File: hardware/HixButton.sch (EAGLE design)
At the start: 16 parts, among them J1 FTDI, J3 XH2P

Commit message: hardware update
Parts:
- removed AWAKE: (no value), jumper:SJ
- removed J3: XH2P, 0_HixField:XH2P
- added C1: 100nF, rcl:C-EUC1206
- added JMP1: (no value), jumper:SJ
- added L1: GRN, led:LEDCHIPLED_1206
- added L2: RED, led:LEDCHIPLED_1206
- added LIFEPO4, WAKE: XH2P, 0_HixField:XH2P
- added R3, R4: 10K, rcl:R-EU_R1206
- added U$1: CN3058E, 0_HixField:CN3058E
- added U1: TPS3839L30, 0_HixField:TPS3839
- added X1: MINI-USB_SHIELD5P4-32005-400, con-cypressindustries:MINI-USB_SHIELD5P4-32005-400
- C2: value 47μF -> 1uF; device rcl:CPOL-EUSMCA -> rcl:C-EUC1206
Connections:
- removed net N$7: R10.1, S3.1, U$2.RST
- new net N$10: C2.1, R4.2, U$1.VIN, X1G$1.1
- new net N$11: L1.A, L2.A, R4.1
- new net N$12: L2.C, U$1.CHRG
- new net N$13: L1.C, U$1.DONE
- new net N$5: R10.1, S3.2, U$2.RST, WAKE.1
- new net N$6: R3.2, U$1.ISET
- new net N$9: S3.1, U1.RST, WAKE.2
- net 3.3V: now also C1.1, LIFEPO4.2, U$1.BAT, U$1.FB, U1.VDD; no longer C2.+, J3.2
- net GND: now also C1.2, C2.2, JMP1.1, LIFEPO4.1, R3.1, U$1.GND, U$1.TEMP, U1.GND, X1G$1.4; no longer AWAKE.1, C2.-, J3.1, S3.2
- net N$4: now also JMP1.2; no longer AWAKE.2
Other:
- moved on the sheet: C3, C5, C6, J1, R1, R10, R11, R12, R2, S3, S4, U$2

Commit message: updated hardware board and schematic
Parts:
- removed U$3: LED_RGB, 0_HixField:LED_RGB
- added U4: LED_RGBWS2812_5050, 0_HixField:LED_RGBWS2812_5050
- R3: value 10K -> 1.2K
- R4: value 10K -> 330
- renumbered U$1 to U2, U$2 to U3
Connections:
- net N$10 renamed VIN
- net 3.3V: now also U4.VCC; no longer U$3.VCC
- net GND: now also U4.GND; no longer U$3.GND
- net RGB: now also U4.DIN; no longer U$3.DIN

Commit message: updated hardware
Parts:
- removed S4: PROG, 0_HixField:PUSHBTNSMALL
- added C10: 1uF, rcl:C-EUC1206
- added C4: 100nF, rcl:C-EUC1206
- added C7, C8, C9: 100μF, rcl:CPOL-EUSMCA
- added PROG: (no value), jumper:SJ
- C2: value 1uF -> 100nF
- C5: value 100nF -> 100μF; device rcl:C-EUC1206 -> rcl:CPOL-EUSMCA; SPICEPREFIX C -> (none)
- C6: value 680μF/6.3V -> 100μF; device 0_HixField:ELCOELKO_RADIAL_STRAIGHT_4P_8D_9H -> rcl:CPOL-EUSMCA
- U1: value TPS3839L30 -> ESP8266(ESP12E)V2; device 0_HixField:TPS3839 -> 0_HixField:ESP8266(ESP12E)V2
- U2: value CN3058E -> TPS3839L30; device 0_HixField:CN3058E -> 0_HixField:TPS3839
- U3: value ESP8266(ESP12E)V2 -> CN3058E; device 0_HixField:ESP8266(ESP12E)V2 -> 0_HixField:CN3058E
- renumbered JMP1 to STAYAWAKE
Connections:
- net 3.3V: now also C2.1, C4.1, C5.+, C7.+, C8.+, C9.+, U1.VCC, U2.VDD, U3.BAT, U3.FB; no longer C5.1, U1.VDD, U2.BAT, U2.FB, U3.VCC
- net GND: now also C10.2, C4.2, C5.-, C7.-, C8.-, C9.-, PROG.1, U3.TEMP; no longer C5.2, S4.2, U2.TEMP
- net N$1: now also U1.CS_TXD2_GPIO15; no longer U3.CS_TXD2_GPIO15
- net N$12: now also U3.CHRG; no longer U2.CHRG
- net N$13: now also U3.DONE; no longer U2.DONE
- net N$2: now also U1.TXD1_GPIO2; no longer U3.TXD1_GPIO2
- net N$3: now also PROG.2, U1.FLASH_GPIO0; no longer S4.1, U3.FLASH_GPIO0
- net N$4: now also U1.SDA_GPIO4; no longer U3.SDA_GPIO4
- net N$5: now also U1.RST; no longer U3.RST
- net N$6: now also U3.ISET; no longer U2.ISET
- net N$8: now also U1.ENABLE; no longer U3.ENABLE
- net N$9: now also U2.RST; no longer U1.RST
- net RGB: now also U1.SCL_GPIO5; no longer U3.SCL_GPIO5
- net RXD: now also U1.TXD0_GPIO1; no longer U3.TXD0_GPIO1
- net TXD: now also U1.RXD0_GPIO3; no longer U3.RXD0_GPIO3
- net VIN: now also C10.1, U3.VIN; no longer C2.1, U2.VIN
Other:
- moved on the sheet: C1, C2, C3, C6, L1, L2, LIFEPO4, R3, R4, X1

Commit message: updated sch and board layout
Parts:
- removed X1: MINI-USB_SHIELD5P4-32005-400, con-cypressindustries:MINI-USB_SHIELD5P4-32005-400
- R3: value 1.2K -> 5.6K
- U4: value LED_RGBWS2812_5050 -> WS2812
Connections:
- removed net VIN: C10.1, R4.2, U3.VIN, X1G$1.1
- new net 5.0V: C10.1, J1.5V, R4.2, U3.VIN
- net 3.3V: no longer J1.5V
- net GND: no longer X1G$1.4
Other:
- moved on the sheet: C10

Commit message: orderd pcbs
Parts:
- renumbered L1 to L1(GRN), L2 to L2(RED)
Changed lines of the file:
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@@
 </part>
 <part name="GND10" library="supply1" library_urn="urn:adsk.eagle:library:371" deviceset="GND" device=""/>
-<part name="L2" library="led" library_urn="urn:adsk.eagle:library:259" deviceset="LED" device="CHIPLED_1206" package3d_urn="urn:adsk.eagle:package:15823/2" value="RED"/>
-<part name="L1" library="led" library_urn="urn:adsk.eagle:library:259" deviceset="LED" device="CHIPLED_1206" package3d_urn="urn:adsk.eagle:package:15823/2" value="GRN"/>
+<part name="L2(RED)" library="led" library_urn="urn:adsk.eagle:library:259" deviceset="LED" device="CHIPLED_1206" package3d_urn="urn:adsk.eagle:package:15823/2" value="RED"/>
+<part name="L1(GRN)" library="led" library_urn="urn:adsk.eagle:library:259" deviceset="LED" device="CHIPLED_1206" package3d_urn="urn:adsk.eagle:package:15823/2" value="GRN"/>
 <part name="R4" library="rcl" library_urn="urn:adsk.eagle:library:334" deviceset="R-EU_" device="R1206" package3d_urn="urn:adsk.eagle:package:23540/2" value="330"/>
 <part name="GND8" library="supply1" library_urn="urn:adsk.eagle:library:371" deviceset="GND" device=""/>
@@
 <attribute name="VALUE" x="60.96" y="68.58" size="1.778" layer="96"/>
 </instance>
-<instance part="L2" gate="G$1" x="86.36" y="101.6" smashed="yes">
+<instance part="L2(RED)" gate="G$1" x="86.36" y="101.6" smashed="yes">
 <attribute name="NAME" x="89.662" y="104.14" size="1.778" layer="95" rot="R180"/>
 <attribute name="VALUE" x="91.948" y="97.663" size="1.778" layer="96" rot="R180"/>
 </instance>
-<instance part="L1" gate="G$1" x="76.2" y="101.6" smashed="yes">
+<instance part="L1(GRN)" gate="G$1" x="76.2" y="101.6" smashed="yes">
 <attribute name="NAME" x="75.184" y="104.14" size="1.778" layer="95" rot="R180"/>
 <attribute name="VALUE" x="75.692" y="97.409" size="1.778" layer="96" rot="R180"/>
@@
 <segment>
 <pinref part="R4" gate="G$1" pin="1"/>
-<pinref part="L2" gate="G$1" pin="A"/>
+<pinref part="L2(RED)" gate="G$1" pin="A"/>
 <wire x1="81.28" y1="104.14" x2="86.36" y2="104.14" width="0.1524" layer="91"/>
-<pinref part="L1" gate="G$1" pin="A"/>
+<pinref part="L1(GRN)" gate="G$1" pin="A"/>
 <wire x1="81.28" y1="104.14" x2="76.2" y2="104.14" width="0.1524" layer="91"/>
 <junction x="81.28" y="104.14"/>
@@
 <net name="N$12" class="2">
 <segment>
-<pinref part="L2" gate="G$1" pin="C"/>
+<pinref part="L2(RED)" gate="G$1" pin="C"/>
 <wire x1="86.36" y1="96.52" x2="86.36" y2="93.98" width="0.1524" layer="91"/>
 <wire x1="86.36" y1="93.98" x2="91.44" y2="93.98" width="0.1524" layer="91"/>
@@
 <net name="N$13" class="2">
 <segment>
-<pinref part="L1" gate="G$1" pin="C"/>
+<pinref part="L1(GRN)" gate="G$1" pin="C"/>
 <wire x1="76.2" y1="96.52" x2="76.2" y2="88.9" width="0.1524" layer="91"/>
 <wire x1="76.2" y1="88.9" x2="91.44" y2="88.9" width="0.1524" layer="91"/>

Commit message: update readme
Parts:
- J1: value FTDI -> FTDIFTDI_ANGLED; device 0_HixField:FTDI -> 0_HixField:FTDIFTDI_ANGLED
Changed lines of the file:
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@@
 <parts>
 <part name="SUPPLY2" library="0_HixField" library_urn="urn:adsk.eagle:library:13392178" deviceset="3.3V" device=""/>
-<part name="J1" library="0_HixField" library_urn="urn:adsk.eagle:library:13392178" deviceset="FTDI" device="" package3d_urn="urn:adsk.eagle:package:12836035/3"/>
+<part name="J1" library="0_HixField" library_urn="urn:adsk.eagle:library:13392178" deviceset="FTDI" device="FTDI_ANGLED" package3d_urn="urn:adsk.eagle:package:25353491/8" value="FTDIFTDI_ANGLED"/>
 <part name="GND3" library="supply1" library_urn="urn:adsk.eagle:library:371" deviceset="GND" device=""/>
 <part name="FRAME1" library="frames" library_urn="urn:adsk.eagle:library:229" deviceset="A4L-LOC" device=""/>

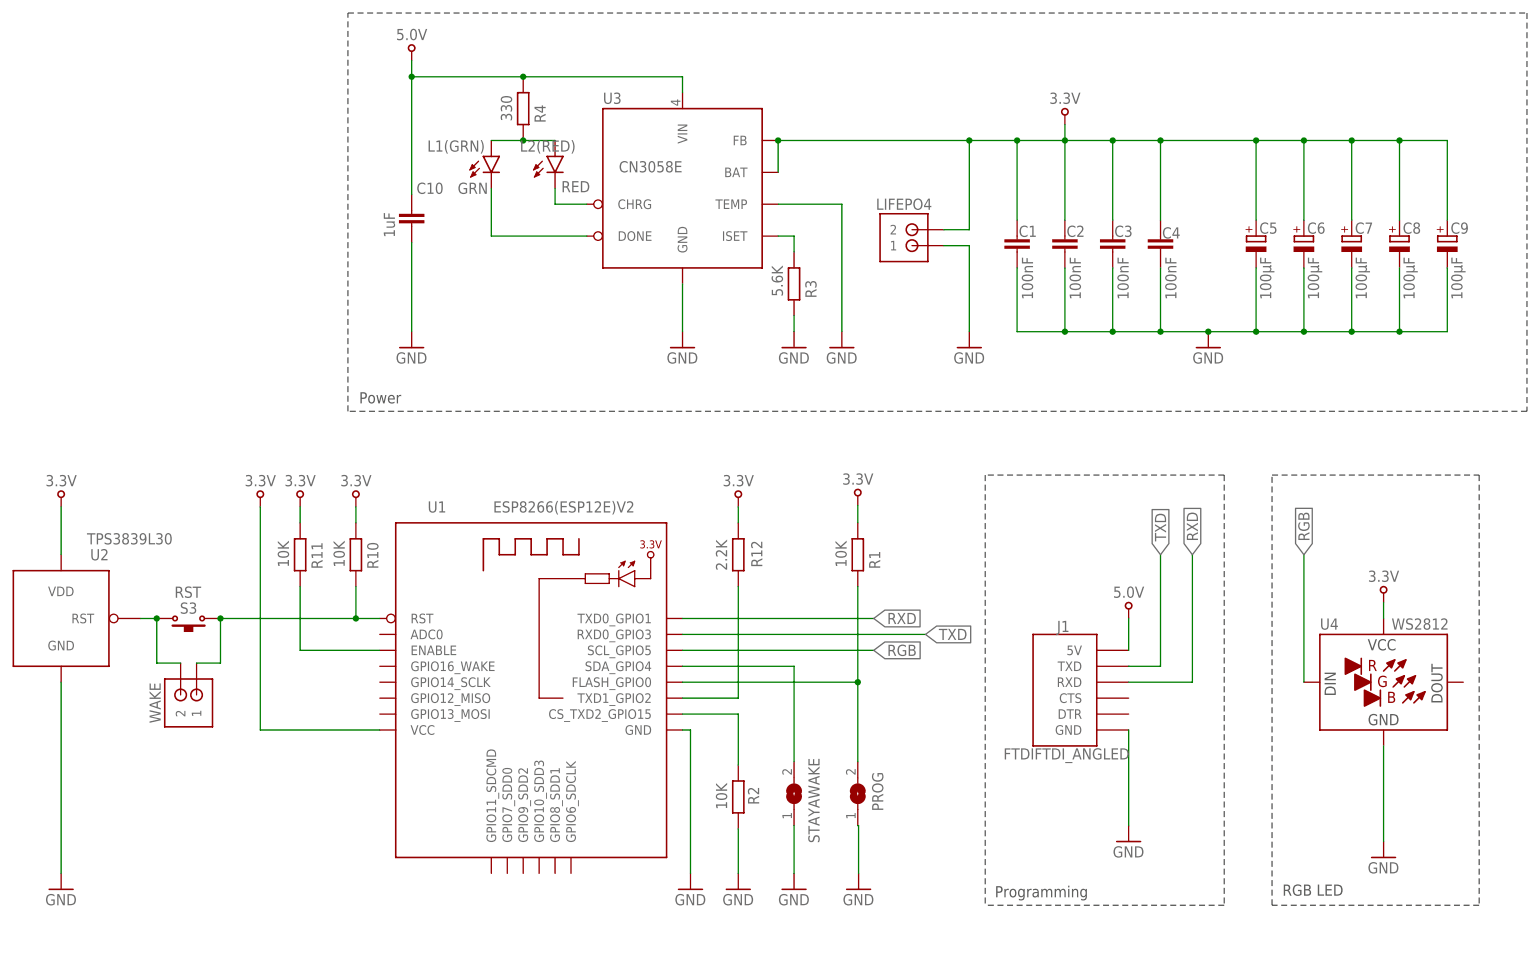
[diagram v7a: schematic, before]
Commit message: v1.1.0 fix voltage supervisor
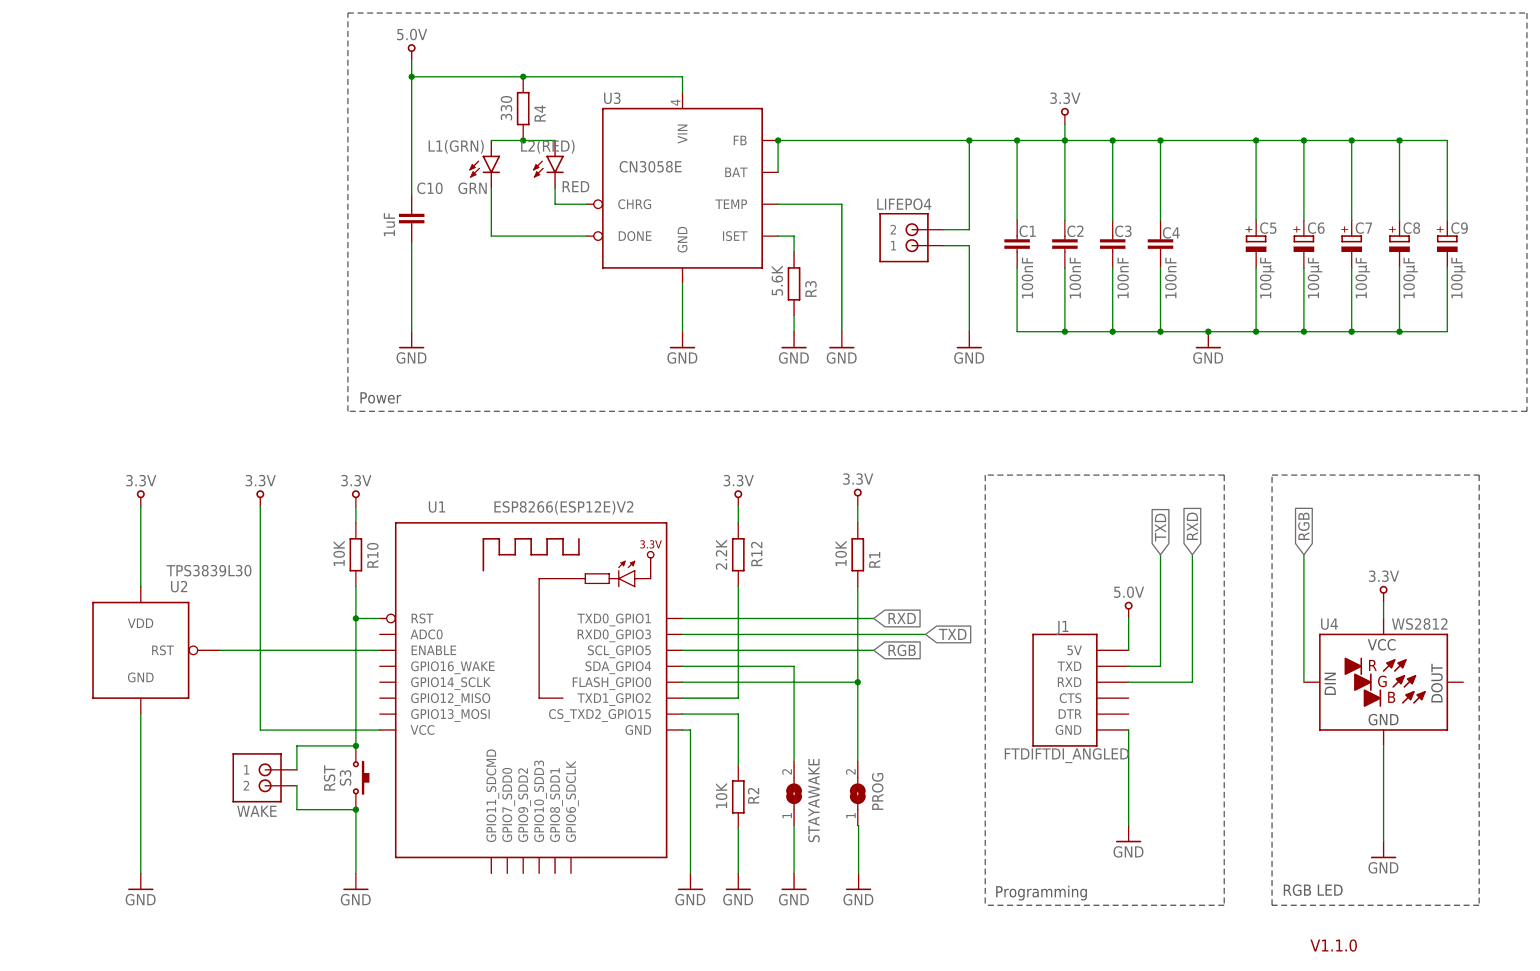
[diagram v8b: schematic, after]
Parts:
- removed R11: 10K, rcl:R-EU_R1206
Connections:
- removed net N$8: R11.1, U1.ENABLE
- removed net N$9: S3.1, U2.RST, WAKE.2
- new net N$7: U1.ENABLE, U2.RST
- net 3.3V: no longer R11.2
- net GND: now also S3.1, WAKE.2
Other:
- note added: "V1.1.0"
- moved on the sheet: S3, U2, WAKE
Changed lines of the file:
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@@
 <part name="R10" library="rcl" library_urn="urn:adsk.eagle:library:334" deviceset="R-EU_" device="R1206" package3d_urn="urn:adsk.eagle:package:23540/2" value="10K"/>
 <part name="SUPPLY15" library="0_HixField" library_urn="urn:adsk.eagle:library:13392178" deviceset="3.3V" device=""/>
-<part name="R11" library="rcl" library_urn="urn:adsk.eagle:library:334" deviceset="R-EU_" device="R1206" package3d_urn="urn:adsk.eagle:package:23540/2" value="10K"/>
-<part name="SUPPLY16" library="0_HixField" library_urn="urn:adsk.eagle:library:13392178" deviceset="3.3V" device=""/>
 <part name="R12" library="rcl" library_urn="urn:adsk.eagle:library:334" deviceset="R-EU_" device="R1206" package3d_urn="urn:adsk.eagle:package:23540/2" value="2.2K"/>
 <part name="SUPPLY17" library="0_HixField" library_urn="urn:adsk.eagle:library:13392178" deviceset="3.3V" device=""/>
@@
 <part name="U3" library="0_HixField" library_urn="urn:adsk.eagle:library:13392178" deviceset="CN3058E" device="" package3d_urn="urn:adsk.eagle:package:25237379/2"/>
 <part name="U4" library="0_HixField" library_urn="urn:adsk.eagle:library:13392178" deviceset="LED_RGB" device="WS2812_5050" package3d_urn="urn:adsk.eagle:package:25237728/2" value="WS2812"/>
+<part name="GND1" library="supply1" library_urn="urn:adsk.eagle:library:371" deviceset="GND" device=""/>
 </parts>
 <sheets>
@@
 <wire x1="233.68" y1="50.8" x2="233.68" y2="-17.78" width="0.1524" layer="97" style="shortdash"/>
 <text x="202.311" y="-16.256" size="1.778" layer="97">RGB LED</text>
+<text x="206.756" y="-25.146" size="1.905" layer="94">V1.1.0</text>
 </plain>
 <instances>
@@
 <attribute name="VALUE" x="39.37" y="49.911" size="1.778" layer="96" align="center"/>
 </instance>
-<instance part="S3" gate="G$1" x="27.94" y="27.94" smashed="yes" rot="R90">
-<attribute name="NAME" x="27.94" y="29.591" size="1.778" layer="95" rot="R180" align="center"/>
-<attribute name="VALUE" x="27.813" y="32.131" size="1.778" layer="96" rot="R180" align="center"/>
+<instance part="S3" gate="G$1" x="54.61" y="2.54" smashed="yes" rot="R180">
+<attribute name="NAME" x="52.959" y="2.54" size="1.778" layer="95" rot="R270" align="center"/>
+<attribute name="VALUE" x="50.419" y="2.413" size="1.778" layer="96" rot="R270" align="center"/>
 </instance>
 <instance part="R10" gate="G$1" x="54.61" y="38.1" smashed="yes" rot="R90">
@@
 <attribute name="VALUE" x="54.61" y="49.911" size="1.778" layer="96" align="center"/>
 </instance>
-<instance part="R11" gate="G$1" x="45.72" y="38.1" smashed="yes" rot="R90">
-<attribute name="NAME" x="49.3014" y="35.814" size="1.778" layer="95" rot="R90"/>
-<attribute name="VALUE" x="43.942" y="36.068" size="1.778" layer="96" rot="R90"/>
-</instance>
-<instance part="SUPPLY16" gate="P" x="45.72" y="48.26" smashed="yes">
-<attribute name="VALUE" x="45.72" y="49.911" size="1.778" layer="96" align="center"/>
-</instance>
 <instance part="R12" gate="G$1" x="115.57" y="38.1" smashed="yes" rot="R90">
 <attribute name="NAME" x="119.4054" y="36.068" size="1.778" layer="95" rot="R90"/>
@@
 <attribute name="NAME" x="141.986" y="93.98" size="1.778" layer="95" rot="R180" align="center"/>
 </instance>
-<instance part="WAKE" gate="J$1" x="26.67" y="15.748" smashed="yes" rot="R270">
-<attribute name="NAME" x="22.606" y="14.478" size="1.778" layer="95" rot="R270" align="center"/>
-</instance>
-<instance part="U2" gate="G$1" x="5.08" y="27.94" smashed="yes">
-<attribute name="NAME" x="15.24" y="38.1" size="1.778" layer="95" align="center-right"/>
-<attribute name="VALUE" x="25.4" y="40.64" size="1.778" layer="96" align="center-right"/>
-</instance>
-<instance part="SUPPLY5" gate="P" x="7.62" y="48.26" smashed="yes">
-<attribute name="VALUE" x="7.62" y="49.911" size="1.778" layer="96" align="center"/>
-</instance>
-<instance part="GND5" gate="1" x="7.62" y="-15.24" smashed="yes">
-<attribute name="VALUE" x="5.08" y="-17.78" size="1.778" layer="96"/>
+<instance part="WAKE" gate="J$1" x="40.132" y="1.27" smashed="yes" rot="MR0">
+<attribute name="NAME" x="38.862" y="-2.794" size="1.778" layer="95" rot="MR0" align="center"/>
+</instance>
+<instance part="U2" gate="G$1" x="17.78" y="22.86" smashed="yes">
+<attribute name="NAME" x="27.94" y="33.02" size="1.778" layer="95" align="center-right"/>
+<attribute name="VALUE" x="38.1" y="35.56" size="1.778" layer="96" align="center-right"/>
+</instance>
+<instance part="SUPPLY5" gate="P" x="20.32" y="48.26" smashed="yes">
+<attribute name="VALUE" x="20.32" y="49.911" size="1.778" layer="96" align="center"/>
+</instance>
+<instance part="GND5" gate="1" x="20.32" y="-15.24" smashed="yes">
+<attribute name="VALUE" x="17.78" y="-17.78" size="1.778" layer="96"/>
 </instance>
 <instance part="R3" gate="G$1" x="124.46" y="81.28" smashed="yes" rot="R90">
@@
 <attribute name="VALUE" x="228.854" y="26.162" size="1.778" layer="96" align="bottom-right"/>
 <attribute name="NAME" x="208.28" y="26.162" size="1.778" layer="95"/>
+</instance>
+<instance part="GND1" gate="1" x="54.61" y="-15.24" smashed="yes">
+<attribute name="VALUE" x="52.07" y="-17.78" size="1.778" layer="96"/>
 </instance>
 </instances>
@@
 <pinref part="GND5" gate="1" pin="GND"/>
 <pinref part="U2" gate="G$1" pin="GND"/>
-<wire x1="7.62" y1="-12.7" x2="7.62" y2="17.78" width="0.1524" layer="91"/>
+<wire x1="20.32" y1="-12.7" x2="20.32" y2="12.7" width="0.1524" layer="91"/>
 </segment>
 <segment>
@@
 <wire x1="132.08" y1="93.98" x2="121.92" y2="93.98" width="0.1524" layer="91"/>
 </segment>
+<segment>
+<pinref part="S3" gate="G$1" pin="1"/>
+<pinref part="WAKE" gate="J$1" pin="2"/>
+<wire x1="45.212" y1="1.27" x2="45.212" y2="-2.54" width="0.1524" layer="91"/>
+<wire x1="45.212" y1="-2.54" x2="54.61" y2="-2.54" width="0.1524" layer="91"/>
+<pinref part="GND1" gate="1" pin="GND"/>
+<wire x1="54.61" y1="-2.54" x2="54.61" y2="-12.7" width="0.1524" layer="91"/>
+<junction x="54.61" y="-2.54"/>
+</segment>
 </net>
 <net name="3.3V" class="1">
@@
 </segment>
 <segment>
-<pinref part="R11" gate="G$1" pin="2"/>
-<wire x1="45.72" y1="43.18" x2="45.72" y2="45.72" width="0.1524" layer="91"/>
-<pinref part="SUPPLY16" gate="P" pin="3.3V"/>
-</segment>
-<segment>
 <pinref part="R12" gate="G$1" pin="2"/>
 <pinref part="SUPPLY17" gate="P" pin="3.3V"/>
@@
 <pinref part="U2" gate="G$1" pin="VDD"/>
 <pinref part="SUPPLY5" gate="P" pin="3.3V"/>
-<wire x1="7.62" y1="38.1" x2="7.62" y2="45.72" width="0.1524" layer="91"/>
+<wire x1="20.32" y1="33.02" x2="20.32" y2="45.72" width="0.1524" layer="91"/>
 </segment>
 <segment>
@@
 </segment>
 </net>
-<net name="N$8" class="2">
-<segment>
-<pinref part="U1" gate="G$1" pin="ENABLE"/>
-<pinref part="R11" gate="G$1" pin="1"/>
-<wire x1="58.42" y1="22.86" x2="45.72" y2="22.86" width="0.1524" layer="91"/>
-<wire x1="45.72" y1="22.86" x2="45.72" y2="33.02" width="0.1524" layer="91"/>
-</segment>
-</net>
 <net name="RGB" class="2">
 <segment>
@@
 </segment>
 </net>
-<net name="N$9" class="2">
-<segment>
-<pinref part="U2" gate="G$1" pin="RST"/>
-<pinref part="S3" gate="G$1" pin="1"/>
-<wire x1="22.86" y1="27.94" x2="20.32" y2="27.94" width="0.1524" layer="91"/>
-<pinref part="WAKE" gate="J$1" pin="2"/>
-<wire x1="26.67" y1="20.828" x2="22.86" y2="20.828" width="0.1524" layer="91"/>
-<wire x1="22.86" y1="20.828" x2="22.86" y2="27.94" width="0.1524" layer="91"/>
-<junction x="22.86" y="27.94"/>
-</segment>
-</net>
 <net name="N$5" class="2">
 <segment>
 <pinref part="S3" gate="G$1" pin="2"/>
 <pinref part="WAKE" gate="J$1" pin="1"/>
-<wire x1="29.21" y1="20.828" x2="33.02" y2="20.828" width="0.1524" layer="91"/>
-<wire x1="33.02" y1="20.828" x2="33.02" y2="27.94" width="0.1524" layer="91"/>
-<junction x="33.02" y="27.94"/>
+<wire x1="45.212" y1="3.81" x2="45.212" y2="7.62" width="0.1524" layer="91"/>
+<wire x1="45.212" y1="7.62" x2="54.61" y2="7.62" width="0.1524" layer="91"/>
+<junction x="54.61" y="7.62"/>
 <wire x1="58.42" y1="27.94" x2="54.61" y2="27.94" width="0.1524" layer="91"/>
 <pinref part="U1" gate="G$1" pin="RST"/>
 <pinref part="R10" gate="G$1" pin="1"/>
-<wire x1="54.61" y1="27.94" x2="33.02" y2="27.94" width="0.1524" layer="91"/>
+<wire x1="54.61" y1="27.94" x2="54.61" y2="7.62" width="0.1524" layer="91"/>
 <wire x1="54.61" y1="33.02" x2="54.61" y2="27.94" width="0.1524" layer="91"/>
 <junction x="54.61" y="27.94"/>
@@
 </segment>
 </net>
+<net name="N$7" class="2">
+<segment>
+<pinref part="U1" gate="G$1" pin="ENABLE"/>
+<pinref part="U2" gate="G$1" pin="RST"/>
+<wire x1="58.42" y1="22.86" x2="33.02" y2="22.86" width="0.1524" layer="91"/>
+</segment>
+</net>
